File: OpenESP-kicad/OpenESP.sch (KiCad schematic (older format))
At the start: 8 parts

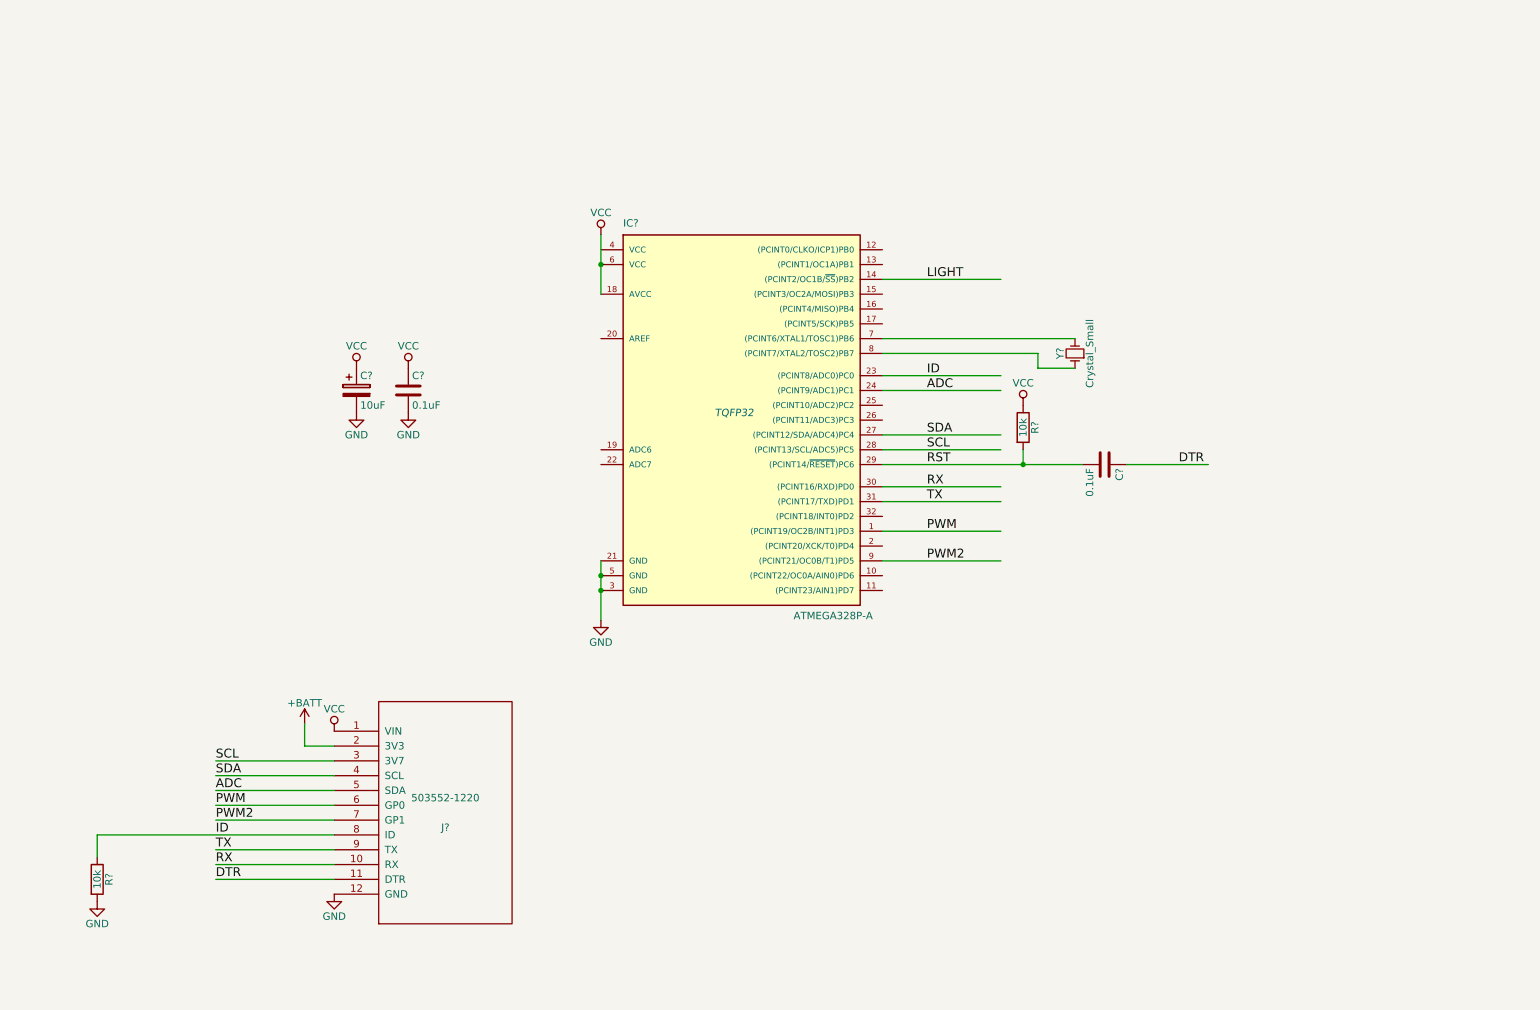
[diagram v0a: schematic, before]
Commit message: added boost converter; changed connector pinout
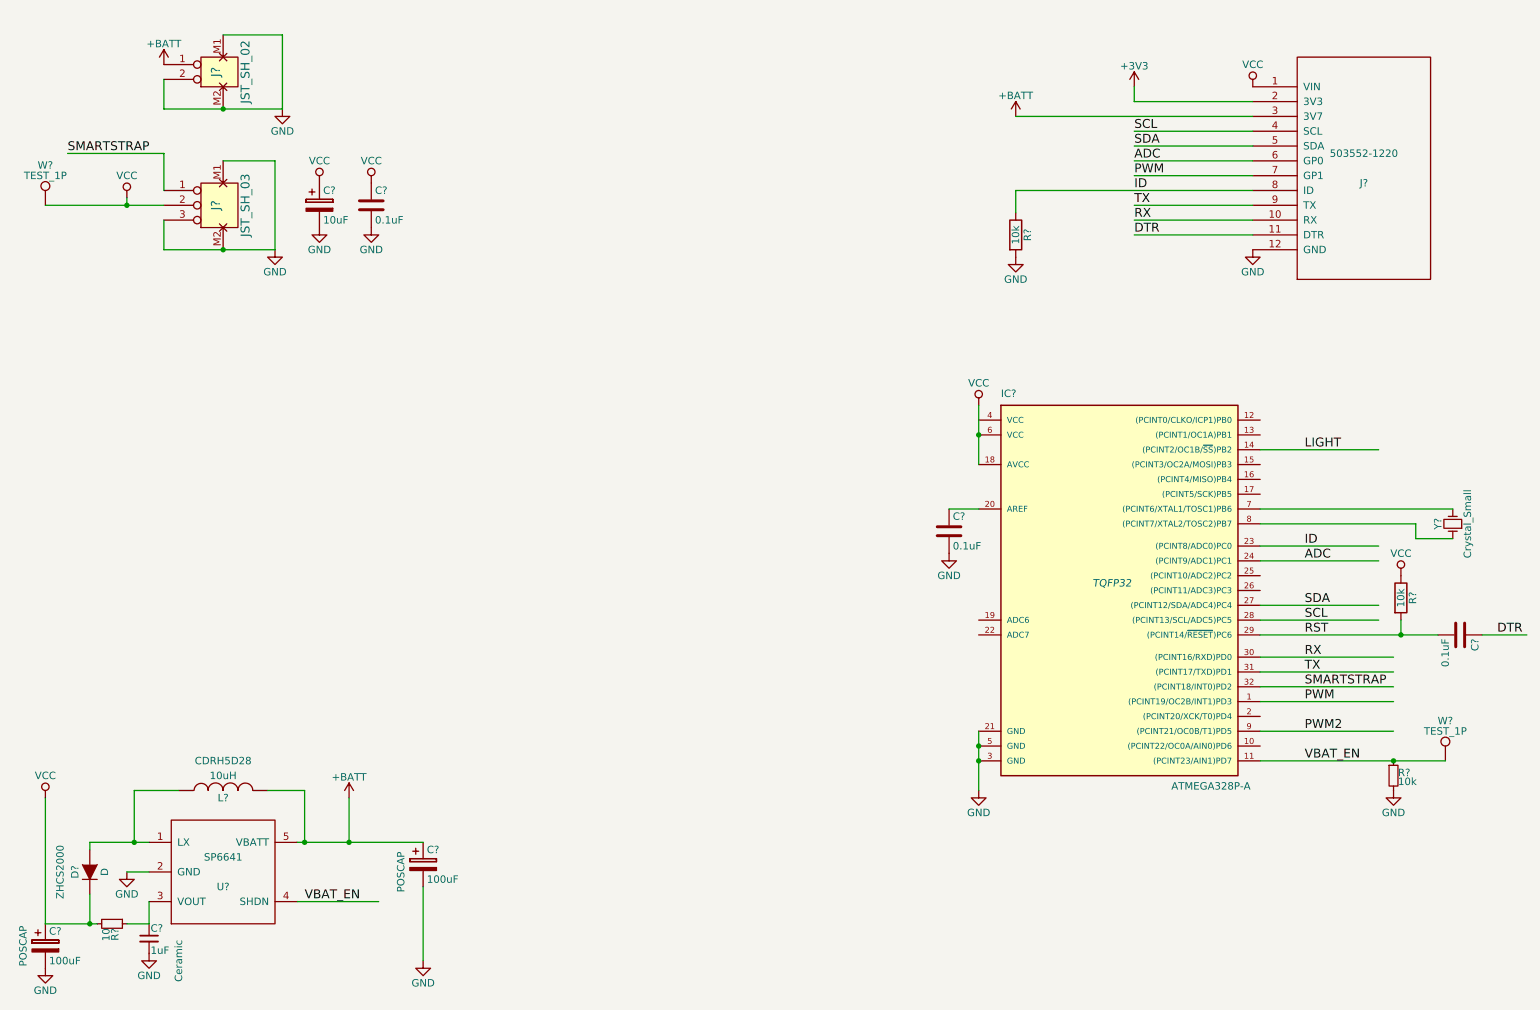
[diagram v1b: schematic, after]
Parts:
- added C?: 0.1uF, symbol C
- added C?: 1uF, symbol C_Small
- added C? (x2): 100uF, symbol CP
- added D?: D, symbol D
- added J?: JST_SH_03, symbol JST_SH_03
- added J?: JST_SH_02, symbol JST_SH_02
- added L?: 10uH, symbol INDUCTOR
- added R?: 10k, symbol R_Small
- added R?: 10, symbol R_Small
- added U?: SP6641, MODULE, symbol SP6641
- added W? (x2): TEST_1P, symbol TEST_1P
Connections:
- net labels added: +3V3, SMARTSTRAP, VBAT_EN
- wire segments 30 -> 61
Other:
- moved on the sheet: C?, IC?, J?, R?, Y?

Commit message: changed LDO regulator
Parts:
- added C? (x2): 0.1uF, symbol C
- added U?: NCP551, MODULE, symbol NCP551
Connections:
- net labels removed: PWM2
- wire segments 61 -> 79
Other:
- note added: "12-pin Molex SlimStack connector"
- note added: "2-pin JST to battery"
- note added: "3-pin JST to Pebble"
- note added: "3.3V Linear Regulator"
- note added: "5V boost regulator"
- note added: "Application Processor"
- moved on the sheet: C?, J?, W?
